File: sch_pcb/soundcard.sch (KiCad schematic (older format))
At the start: 50 parts, among them U501 CM108B, U502 CM108B, U503 TUSB2036, Y501 6MHz

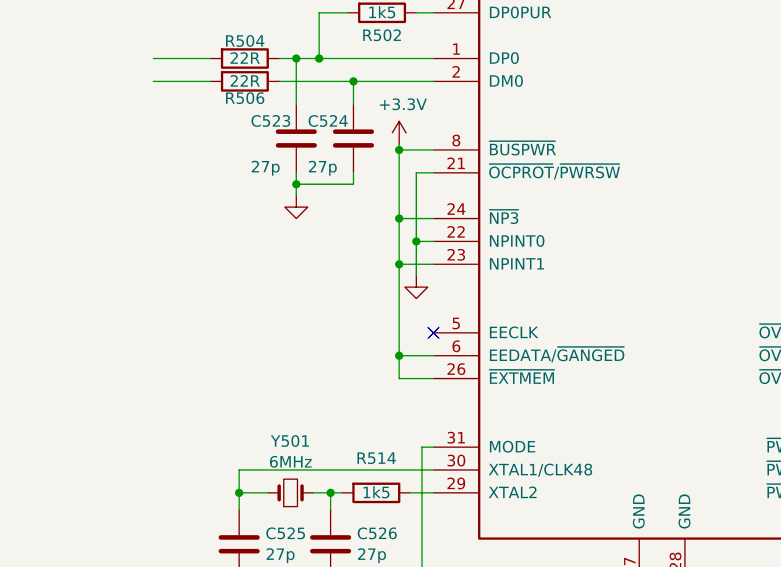
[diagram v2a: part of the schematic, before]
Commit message: Add files via upload
More routing of the PCB....  Slowly getting there.
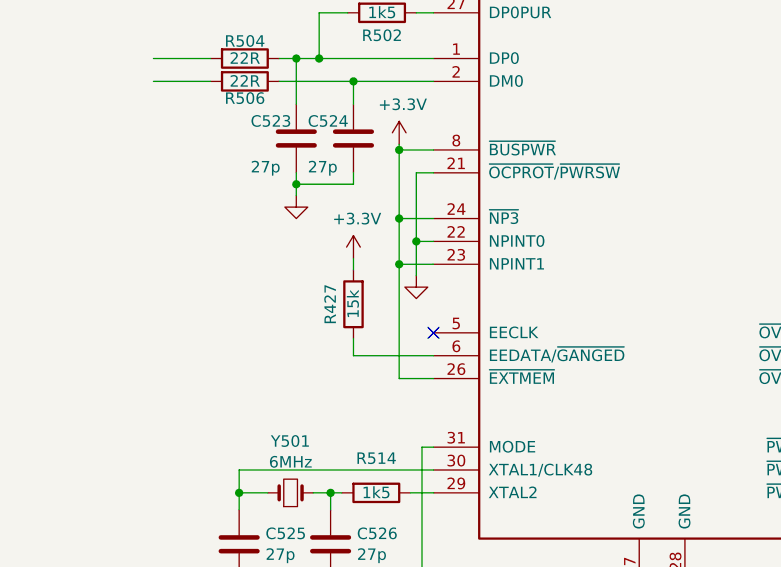
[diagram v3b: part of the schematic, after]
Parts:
- added R427: 15k, lib:smd0603, symbol R
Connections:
- wire segments 169 -> 171
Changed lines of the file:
@@
 LIBS:conn
 LIBS:PiPtr-cache
-EELAYER 25 0
+EELAYER 26 0
 EELAYER END
 $Descr A4 11693 8268
@@
 	9775 2125 9775 2200
 $Comp
-L GND #PWR0149
+L GND #PWR0148
 U 1 1 5968E48D
 P 9775 2200
-F 0 "#PWR0149" H 9775 1950 50  0001 C CNN
+F 0 "#PWR0148" H 9775 1950 50  0001 C CNN
 F 1 "GND" H 9780 2027 50  0001 C CNN
 F 2 "" H 9775 2200 50  0001 C CNN
@@
 $EndComp
 $Comp
-L GND #PWR0150
+L GND #PWR0149
 U 1 1 5968E4AC
 P 8575 4025
-F 0 "#PWR0150" H 8575 3775 50  0001 C CNN
+F 0 "#PWR0149" H 8575 3775 50  0001 C CNN
 F 1 "GND" H 8580 3852 50  0001 C CNN
 F 2 "" H 8575 4025 50  0001 C CNN
@@
 Connection ~ 8275 3925
 $Comp
-L GND #PWR0151
+L GND #PWR0150
 U 1 1 5968E5A1
 P 7100 3550
-F 0 "#PWR0151" H 7100 3300 50  0001 C CNN
+F 0 "#PWR0150" H 7100 3300 50  0001 C CNN
 F 1 "GND" H 7105 3377 50  0001 C CNN
 F 2 "" H 7100 3550 50  0001 C CNN
@@
 $EndComp
 $Comp
-L GND #PWR0152
+L GND #PWR0151
 U 1 1 5968EB73
 P 6925 1525
-F 0 "#PWR0152" H 6925 1275 50  0001 C CNN
+F 0 "#PWR0151" H 6925 1275 50  0001 C CNN
 F 1 "GND" H 6930 1352 50  0001 C CNN
 F 2 "" H 6925 1525 50  0001 C CNN
@@
 $EndComp
 $Comp
-L GND #PWR0153
+L GND #PWR0152
 U 1 1 5968F4FA
 P 9775 3975
-F 0 "#PWR0153" H 9775 3725 50  0001 C CNN
+F 0 "#PWR0152" H 9775 3725 50  0001 C CNN
 F 1 "GND" H 9780 3802 50  0001 C CNN
 F 2 "" H 9775 3975 50  0001 C CNN
@@
 Connection ~ 6200 4000
 $Comp
-L GND #PWR0154
+L GND #PWR0153
 U 1 1 5968FE8C
 P 6200 4075
-F 0 "#PWR0154" H 6200 3825 50  0001 C CNN
+F 0 "#PWR0153" H 6200 3825 50  0001 C CNN
 F 1 "GND" H 6205 3902 50  0001 C CNN
 F 2 "" H 6200 4075 50  0001 C CNN
@@
 	4525 2125 4525 2200
 $Comp
-L GND #PWR0155
+L GND #PWR0154
 U 1 1 596926E6
 P 4525 2200
-F 0 "#PWR0155" H 4525 1950 50  0001 C CNN
+F 0 "#PWR0154" H 4525 1950 50  0001 C CNN
 F 1 "GND" H 4530 2027 50  0001 C CNN
 F 2 "" H 4525 2200 50  0001 C CNN
@@
 $EndComp
 $Comp
-L GND #PWR0156
+L GND #PWR0155
 U 1 1 596926EC
 P 3325 4025
-F 0 "#PWR0156" H 3325 3775 50  0001 C CNN
+F 0 "#PWR0155" H 3325 3775 50  0001 C CNN
 F 1 "GND" H 3330 3852 50  0001 C CNN
 F 2 "" H 3325 4025 50  0001 C CNN
@@
 Connection ~ 3025 3925
 $Comp
-L GND #PWR0157
+L GND #PWR0156
 U 1 1 596926FD
 P 1850 3550
-F 0 "#PWR0157" H 1850 3300 50  0001 C CNN
+F 0 "#PWR0156" H 1850 3300 50  0001 C CNN
 F 1 "GND" H 1855 3377 50  0001 C CNN
 F 2 "" H 1850 3550 50  0001 C CNN
@@
 $EndComp
 $Comp
-L GND #PWR0158
+L GND #PWR0157
 U 1 1 5969275D
 P 4525 3975
-F 0 "#PWR0158" H 4525 3725 50  0001 C CNN
+F 0 "#PWR0157" H 4525 3725 50  0001 C CNN
 F 1 "GND" H 4530 3802 50  0001 C CNN
 F 2 "" H 4525 3975 50  0001 C CNN
@@
 Connection ~ 950  4000
 $Comp
-L GND #PWR0159
+L GND #PWR0158
 U 1 1 59692791
 P 950 4075
-F 0 "#PWR0159" H 950 3825 50  0001 C CNN
+F 0 "#PWR0158" H 950 3825 50  0001 C CNN
 F 1 "GND" H 955 3902 50  0001 C CNN
 F 2 "" H 950 4075 50  0001 C CNN
@@
 $EndComp
 $Comp
-L GND #PWR0160
+L GND #PWR0159
 U 1 1 59695E9D
 P 1750 7675
-F 0 "#PWR0160" H 1750 7425 50  0001 C CNN
+F 0 "#PWR0159" H 1750 7425 50  0001 C CNN
 F 1 "GND" H 1755 7502 50  0001 C CNN
 F 2 "" H 1750 7675 50  0001 C CNN
@@
 NoConn ~ 2600 6500
 $Comp
-L +3.3V #PWR0161
+L +3.3V #PWR0160
 U 1 1 596973F4
 P 2450 5675
-F 0 "#PWR0161" H 2450 5525 50  0001 C CNN
+F 0 "#PWR0160" H 2450 5525 50  0001 C CNN
 F 1 "+3.3V" H 2465 5848 50  0000 C CNN
 F 2 "" H 2450 5675 50  0001 C CNN
@@
 $EndComp
 $Comp
-L GND #PWR0162
+L GND #PWR0161
 U 1 1 596977E6
 P 2525 6250
-F 0 "#PWR0162" H 2525 6000 50  0001 C CNN
+F 0 "#PWR0161" H 2525 6000 50  0001 C CNN
 F 1 "GND" H 2530 6077 50  0001 C CNN
 F 2 "" H 2525 6250 50  0001 C CNN
@@
 Wire Wire Line
 	2525 5800 2600 5800
-Wire Wire Line
-	2600 6600 2450 6600
-Connection ~ 2450 6600
 Wire Wire Line
 	2600 5700 2450 5700
@@
 $EndComp
 $Comp
-L GND #PWR0163
+L GND #PWR0162
 U 1 1 596992AD
 P 2000 5900
-F 0 "#PWR0163" H 2000 5650 50  0001 C CNN
+F 0 "#PWR0162" H 2000 5650 50  0001 C CNN
 F 1 "GND" H 2005 5727 50  0001 C CNN
 F 2 "" H 2000 5900 50  0001 C CNN
@@
 $EndComp
 $Comp
-L GND #PWR0164
+L GND #PWR0163
 U 1 1 5969AB36
 P 4400 4400
-F 0 "#PWR0164" H 4400 4150 50  0001 C CNN
+F 0 "#PWR0163" H 4400 4150 50  0001 C CNN
 F 1 "GND" H 4405 4227 50  0001 C CNN
 F 2 "" H 4400 4400 50  0001 C CNN
@@
 Connection ~ 3500 4325
 $Comp
-L +3.3V #PWR0165
+L +3.3V #PWR0164
 U 1 1 5969B1EB
 P 3500 4250
-F 0 "#PWR0165" H 3500 4100 50  0001 C CNN
+F 0 "#PWR0164" H 3500 4100 50  0001 C CNN
 F 1 "+3.3V" H 3515 4423 50  0000 C CNN
 F 2 "" H 3500 4250 50  0001 C CNN
@@
 NoConn ~ 4600 6100
 Wire Wire Line
-	2600 6200 2450 6200
+	2450 6200 2600 6200
 Connection ~ 2450 6200
 Wire Wire Line
@@
 Connection ~ 5750 6300
 $Comp
-L GND #PWR0166
+L GND #PWR0165
 U 1 1 596A65D7
 P 5750 6375
-F 0 "#PWR0166" H 5750 6125 50  0001 C CNN
+F 0 "#PWR0165" H 5750 6125 50  0001 C CNN
 F 1 "GND" H 5755 6202 50  0001 C CNN
 F 2 "" H 5750 6375 50  0001 C CNN
@@
 $EndComp
 $Comp
-L GND #PWR0167
+L GND #PWR0166
 U 1 1 596AA48C
 P 2200 4900
-F 0 "#PWR0167" H 2200 4650 50  0001 C CNN
+F 0 "#PWR0166" H 2200 4650 50  0001 C CNN
 F 1 "GND" H 2205 4727 50  0001 C CNN
 F 2 "" H 2200 4900 50  0001 C CNN
@@
 $EndComp
 $Comp
-L +3.3V #PWR0168
+L +3.3V #PWR0167
 U 1 1 596AA4FD
 P 2200 4075
-F 0 "#PWR0168" H 2200 3925 50  0001 C CNN
+F 0 "#PWR0167" H 2200 3925 50  0001 C CNN
 F 1 "+3.3V" H 2215 4248 50  0000 C CNN
 F 2 "" H 2200 4075 50  0001 C CNN
@@
 	4775 6125 4775 6050
 $Comp
-L +3.3V #PWR0169
+L +3.3V #PWR0168
 U 1 1 5978D82E
 P 4775 6050
-F 0 "#PWR0169" H 4775 5900 50  0001 C CNN
+F 0 "#PWR0168" H 4775 5900 50  0001 C CNN
 F 1 "+3.3V" H 4790 6223 50  0000 C CNN
 F 2 "" H 4775 6050 50  0001 C CNN
@@
 	10050 3225 10150 3225
 $Comp
-L +5V #PWR0170
+L +5V #PWR0169
 U 1 1 597E7379
 P 6025 850
-F 0 "#PWR0170" H 6025 700 50  0001 C CNN
+F 0 "#PWR0169" H 6025 700 50  0001 C CNN
 F 1 "+5V" H 6025 990 50  0000 C CNN
 F 2 "" H 6025 850 50  0001 C CNN
@@
 $EndComp
 $Comp
-L +5V #PWR0171
+L +5V #PWR0170
 U 1 1 597E7689
 P 875 825
-F 0 "#PWR0171" H 875 675 50  0001 C CNN
+F 0 "#PWR0170" H 875 675 50  0001 C CNN
 F 1 "+5V" H 875 965 50  0000 C CNN
 F 2 "" H 875 825 50  0001 C CNN
@@
 $EndComp
 $Comp
-L +5V #PWR0172
+L +5V #PWR0171
 U 1 1 597C24B2
 P 3075 850
-F 0 "#PWR0172" H 3075 700 50  0001 C CNN
+F 0 "#PWR0171" H 3075 700 50  0001 C CNN
 F 1 "+5V" H 3075 990 50  0000 C CNN
 F 2 "" H 3075 850 50  0001 C CNN
@@
 Connection ~ 9850 1375
 $Comp
-L GND #PWR0173
+L GND #PWR0172
 U 1 1 597C4F1B
 P 9850 1475
-F 0 "#PWR0173" H 9850 1225 50  0001 C CNN
+F 0 "#PWR0172" H 9850 1225 50  0001 C CNN
 F 1 "GND" H 9855 1302 50  0001 C CNN
 F 2 "" H 9850 1475 50  0001 C CNN
@@
 $EndComp
 $Comp
-L GND #PWR0174
+L GND #PWR0173
 U 1 1 597C5606
 P 4750 1450
-F 0 "#PWR0174" H 4750 1200 50  0001 C CNN
+F 0 "#PWR0173" H 4750 1200 50  0001 C CNN
 F 1 "GND" H 4755 1277 50  0001 C CNN
 F 2 "" H 4750 1450 50  0001 C CNN
@@
 Connection ~ 1300 925
 $Comp
-L GND #PWR0175
+L GND #PWR0174
 U 1 1 597C7ACB
 P 1300 1475
-F 0 "#PWR0175" H 1300 1225 50  0001 C CNN
+F 0 "#PWR0174" H 1300 1225 50  0001 C CNN
 F 1 "GND" H 1305 1302 50  0001 C CNN
 F 2 "" H 1300 1475 50  0001 C CNN
@@
 	2775 925  2775 1025
 $Comp
-L +5V #PWR0176
+L +5V #PWR0175
 U 1 1 5982DF1C
 P 8325 850
-F 0 "#PWR0176" H 8325 700 50  0001 C CNN
+F 0 "#PWR0175" H 8325 700 50  0001 C CNN
 F 1 "+5V" H 8325 990 50  0000 C CNN
 F 2 "" H 8325 850 50  0001 C CNN
@@
 Connection ~ 8325 925
 $Comp
-L PWR_FLAG #FLG0177
+L PWR_FLAG #FLG0176
 U 1 1 5982F39E
 P 6925 925
-F 0 "#FLG0177" H 6925 1000 50  0001 C CNN
+F 0 "#FLG0176" H 6925 1000 50  0001 C CNN
 F 1 "PWR_FLAG" H 6925 1099 50  0001 C CNN
 F 2 "" H 6925 925 50  0001 C CNN
@@
 $EndComp
 $Comp
-L PWR_FLAG #FLG0178
+L PWR_FLAG #FLG0177
 U 1 1 5982F5DB
 P 1750 925
-F 0 "#FLG0178" H 1750 1000 50  0001 C CNN
+F 0 "#FLG0177" H 1750 1000 50  0001 C CNN
 F 1 "PWR_FLAG" H 1750 1099 50  0001 C CNN
 F 2 "" H 1750 925 50  0001 C CNN
@@
 	1    0    0    -1
 $EndComp
+$Comp
+L R R427
+U 1 1 59814A45
+P 2250 6375
+F 0 "R427" V 2350 6375 50  0000 C CNN
+F 1 "15k" V 2250 6375 50  0000 C CNN
+F 2 "lib:smd0603" V 2180 6375 50  0001 C CNN
+F 3 "" H 2250 6375 50  0001 C CNN
+	1    2250 6375
+	-1   0    0    1
+$EndComp
+$Comp
+L +3.3V #PWR0401
+U 1 1 59814E80
+P 2250 6175
+F 0 "#PWR0401" H 2250 6025 50  0001 C CNN
+F 1 "+3.3V" H 2265 6348 50  0000 C CNN
+F 2 "" H 2250 6175 50  0001 C CNN
+F 3 "" H 2250 6175 50  0001 C CNN
+	1    2250 6175
+	1    0    0    -1
+$EndComp
+Wire Wire Line
+	2250 6175 2250 6225
+Wire Wire Line
+	2600 6600 2250 6600
+Wire Wire Line
+	2250 6600 2250 6525
 $EndSCHEMATC

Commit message: Add files via upload
Remove OLED connector
Remove extra bypass cap from third EEPOT
More routing - got the soundcards and usb hub done.  Only remaining big section is the DC-DC.  Still a bit of pain-in-the-tuchas traces that need to sneak across the board...
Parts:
- renumbered R427 to R517
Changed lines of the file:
@@
 $EndComp
 $Comp
-L R R427
+L R R517
 U 1 1 59814A45
 P 2250 6375
-F 0 "R427" V 2350 6375 50  0000 C CNN
+F 0 "R517" V 2350 6375 50  0000 C CNN
 F 1 "15k" V 2250 6375 50  0000 C CNN
 F 2 "lib:smd0603" V 2180 6375 50  0001 C CNN

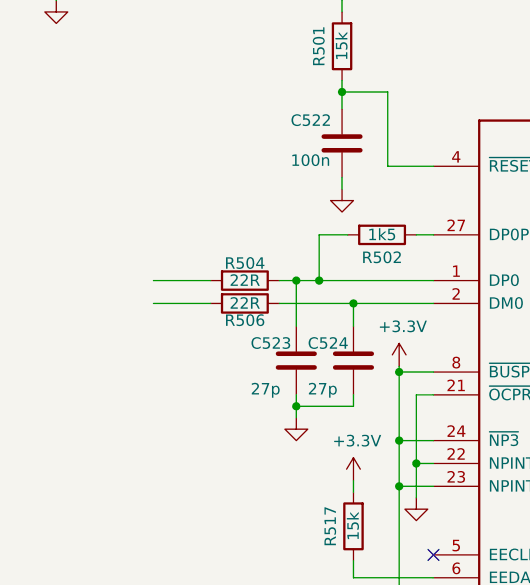
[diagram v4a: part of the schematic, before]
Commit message: Add files via upload
Add USB connector.  Pull back corner of board for it so the main board connector is around the same depth as the one on the Pi
Finish moving all refdes to avoid pads, other silk, and vias
Some routing cleanup
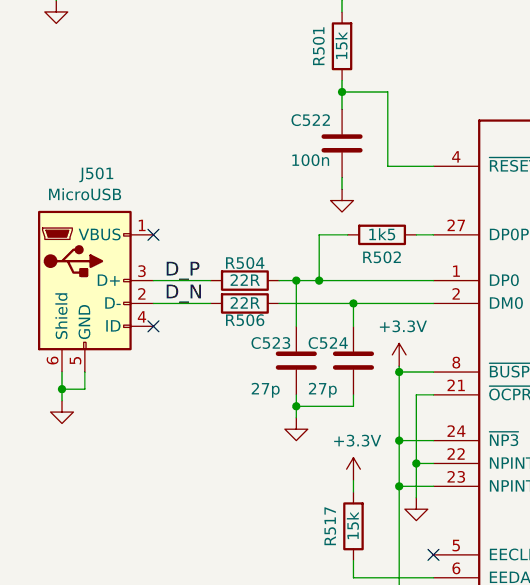
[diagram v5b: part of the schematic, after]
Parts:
- added J501: MicroUSB, lib:USB_Micro-B, symbol USB_OTG
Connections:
- net labels added: D_N, D_P
- wire segments 171 -> 174
- no-connect marks 56 -> 58
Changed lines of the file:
@@
 $Descr A4 11693 8268
 encoding utf-8
-Sheet 4 5
+Sheet 5 5
 Title ""
 Date ""
@@
 	9775 2125 9775 2200
 $Comp
-L GND #PWR0148
+L GND #PWR0182
 U 1 1 5968E48D
 P 9775 2200
-F 0 "#PWR0148" H 9775 1950 50  0001 C CNN
+F 0 "#PWR0182" H 9775 1950 50  0001 C CNN
 F 1 "GND" H 9780 2027 50  0001 C CNN
 F 2 "" H 9775 2200 50  0001 C CNN
@@
 $EndComp
 $Comp
-L GND #PWR0149
+L GND #PWR0183
 U 1 1 5968E4AC
 P 8575 4025
-F 0 "#PWR0149" H 8575 3775 50  0001 C CNN
+F 0 "#PWR0183" H 8575 3775 50  0001 C CNN
 F 1 "GND" H 8580 3852 50  0001 C CNN
 F 2 "" H 8575 4025 50  0001 C CNN
@@
 Connection ~ 8275 3925
 $Comp
-L GND #PWR0150
+L GND #PWR0184
 U 1 1 5968E5A1
 P 7100 3550
-F 0 "#PWR0150" H 7100 3300 50  0001 C CNN
+F 0 "#PWR0184" H 7100 3300 50  0001 C CNN
 F 1 "GND" H 7105 3377 50  0001 C CNN
 F 2 "" H 7100 3550 50  0001 C CNN
@@
 $EndComp
 $Comp
-L GND #PWR0151
+L GND #PWR0185
 U 1 1 5968EB73
 P 6925 1525
-F 0 "#PWR0151" H 6925 1275 50  0001 C CNN
+F 0 "#PWR0185" H 6925 1275 50  0001 C CNN
 F 1 "GND" H 6930 1352 50  0001 C CNN
 F 2 "" H 6925 1525 50  0001 C CNN
@@
 $EndComp
 $Comp
-L GND #PWR0152
+L GND #PWR0186
 U 1 1 5968F4FA
 P 9775 3975
-F 0 "#PWR0152" H 9775 3725 50  0001 C CNN
+F 0 "#PWR0186" H 9775 3725 50  0001 C CNN
 F 1 "GND" H 9780 3802 50  0001 C CNN
 F 2 "" H 9775 3975 50  0001 C CNN
@@
 Connection ~ 6200 4000
 $Comp
-L GND #PWR0153
+L GND #PWR0187
 U 1 1 5968FE8C
 P 6200 4075
-F 0 "#PWR0153" H 6200 3825 50  0001 C CNN
+F 0 "#PWR0187" H 6200 3825 50  0001 C CNN
 F 1 "GND" H 6205 3902 50  0001 C CNN
 F 2 "" H 6200 4075 50  0001 C CNN
@@
 	4525 2125 4525 2200
 $Comp
-L GND #PWR0154
+L GND #PWR0188
 U 1 1 596926E6
 P 4525 2200
-F 0 "#PWR0154" H 4525 1950 50  0001 C CNN
+F 0 "#PWR0188" H 4525 1950 50  0001 C CNN
 F 1 "GND" H 4530 2027 50  0001 C CNN
 F 2 "" H 4525 2200 50  0001 C CNN
@@
 $EndComp
 $Comp
-L GND #PWR0155
+L GND #PWR0189
 U 1 1 596926EC
 P 3325 4025
-F 0 "#PWR0155" H 3325 3775 50  0001 C CNN
+F 0 "#PWR0189" H 3325 3775 50  0001 C CNN
 F 1 "GND" H 3330 3852 50  0001 C CNN
 F 2 "" H 3325 4025 50  0001 C CNN
@@
 Connection ~ 3025 3925
 $Comp
-L GND #PWR0156
+L GND #PWR0190
 U 1 1 596926FD
 P 1850 3550
-F 0 "#PWR0156" H 1850 3300 50  0001 C CNN
+F 0 "#PWR0190" H 1850 3300 50  0001 C CNN
 F 1 "GND" H 1855 3377 50  0001 C CNN
 F 2 "" H 1850 3550 50  0001 C CNN
@@
 $EndComp
 $Comp
-L GND #PWR0157
+L GND #PWR0191
 U 1 1 5969275D
 P 4525 3975
-F 0 "#PWR0157" H 4525 3725 50  0001 C CNN
+F 0 "#PWR0191" H 4525 3725 50  0001 C CNN
 F 1 "GND" H 4530 3802 50  0001 C CNN
 F 2 "" H 4525 3975 50  0001 C CNN
@@
 Connection ~ 950  4000
 $Comp
-L GND #PWR0158
+L GND #PWR0192
 U 1 1 59692791
 P 950 4075
-F 0 "#PWR0158" H 950 3825 50  0001 C CNN
+F 0 "#PWR0192" H 950 3825 50  0001 C CNN
 F 1 "GND" H 955 3902 50  0001 C CNN
 F 2 "" H 950 4075 50  0001 C CNN
@@
 $EndComp
 $Comp
-L GND #PWR0159
+L GND #PWR0193
 U 1 1 59695E9D
 P 1750 7675
-F 0 "#PWR0159" H 1750 7425 50  0001 C CNN
+F 0 "#PWR0193" H 1750 7425 50  0001 C CNN
 F 1 "GND" H 1755 7502 50  0001 C CNN
 F 2 "" H 1750 7675 50  0001 C CNN
@@
 NoConn ~ 2600 6500
 $Comp
-L +3.3V #PWR0160
+L +3.3V #PWR0194
 U 1 1 596973F4
 P 2450 5675
-F 0 "#PWR0160" H 2450 5525 50  0001 C CNN
+F 0 "#PWR0194" H 2450 5525 50  0001 C CNN
 F 1 "+3.3V" H 2465 5848 50  0000 C CNN
 F 2 "" H 2450 5675 50  0001 C CNN
@@
 $EndComp
 $Comp
-L GND #PWR0161
+L GND #PWR0195
 U 1 1 596977E6
 P 2525 6250
-F 0 "#PWR0161" H 2525 6000 50  0001 C CNN
+F 0 "#PWR0195" H 2525 6000 50  0001 C CNN
 F 1 "GND" H 2530 6077 50  0001 C CNN
 F 2 "" H 2525 6250 50  0001 C CNN
@@
 $EndComp
 $Comp
-L GND #PWR0162
+L GND #PWR0196
 U 1 1 596992AD
 P 2000 5900
-F 0 "#PWR0162" H 2000 5650 50  0001 C CNN
+F 0 "#PWR0196" H 2000 5650 50  0001 C CNN
 F 1 "GND" H 2005 5727 50  0001 C CNN
 F 2 "" H 2000 5900 50  0001 C CNN
@@
 $EndComp
 $Comp
-L GND #PWR0163
+L GND #PWR0197
 U 1 1 5969AB36
 P 4400 4400
-F 0 "#PWR0163" H 4400 4150 50  0001 C CNN
+F 0 "#PWR0197" H 4400 4150 50  0001 C CNN
 F 1 "GND" H 4405 4227 50  0001 C CNN
 F 2 "" H 4400 4400 50  0001 C CNN
@@
 Connection ~ 3500 4325
 $Comp
-L +3.3V #PWR0164
+L +3.3V #PWR0198
 U 1 1 5969B1EB
 P 3500 4250
-F 0 "#PWR0164" H 3500 4100 50  0001 C CNN
+F 0 "#PWR0198" H 3500 4100 50  0001 C CNN
 F 1 "+3.3V" H 3515 4423 50  0000 C CNN
 F 2 "" H 3500 4250 50  0001 C CNN
@@
 Connection ~ 5750 6300
 $Comp
-L GND #PWR0165
+L GND #PWR0199
 U 1 1 596A65D7
 P 5750 6375
-F 0 "#PWR0165" H 5750 6125 50  0001 C CNN
+F 0 "#PWR0199" H 5750 6125 50  0001 C CNN
 F 1 "GND" H 5755 6202 50  0001 C CNN
 F 2 "" H 5750 6375 50  0001 C CNN
@@
 $EndComp
 $Comp
-L GND #PWR0166
+L GND #PWR0200
 U 1 1 596AA48C
 P 2200 4900
-F 0 "#PWR0166" H 2200 4650 50  0001 C CNN
+F 0 "#PWR0200" H 2200 4650 50  0001 C CNN
 F 1 "GND" H 2205 4727 50  0001 C CNN
 F 2 "" H 2200 4900 50  0001 C CNN
@@
 $EndComp
 $Comp
-L +3.3V #PWR0167
+L +3.3V #PWR0201
 U 1 1 596AA4FD
 P 2200 4075
-F 0 "#PWR0167" H 2200 3925 50  0001 C CNN
+F 0 "#PWR0201" H 2200 3925 50  0001 C CNN
 F 1 "+3.3V" H 2215 4248 50  0000 C CNN
 F 2 "" H 2200 4075 50  0001 C CNN
@@
 	4775 6125 4775 6050
 $Comp
-L +3.3V #PWR0168
+L +3.3V #PWR0202
 U 1 1 5978D82E
 P 4775 6050
-F 0 "#PWR0168" H 4775 5900 50  0001 C CNN
+F 0 "#PWR0202" H 4775 5900 50  0001 C CNN
 F 1 "+3.3V" H 4790 6223 50  0000 C CNN
 F 2 "" H 4775 6050 50  0001 C CNN
@@
 	10050 3225 10150 3225
 $Comp
-L +5V #PWR0169
+L +5V #PWR0203
 U 1 1 597E7379
 P 6025 850
-F 0 "#PWR0169" H 6025 700 50  0001 C CNN
+F 0 "#PWR0203" H 6025 700 50  0001 C CNN
 F 1 "+5V" H 6025 990 50  0000 C CNN
 F 2 "" H 6025 850 50  0001 C CNN
@@
 $EndComp
 $Comp
-L +5V #PWR0170
+L +5V #PWR0204
 U 1 1 597E7689
 P 875 825
-F 0 "#PWR0170" H 875 675 50  0001 C CNN
+F 0 "#PWR0204" H 875 675 50  0001 C CNN
 F 1 "+5V" H 875 965 50  0000 C CNN
 F 2 "" H 875 825 50  0001 C CNN
@@
 $EndComp
 $Comp
-L +5V #PWR0171
+L +5V #PWR0205
 U 1 1 597C24B2
 P 3075 850
-F 0 "#PWR0171" H 3075 700 50  0001 C CNN
+F 0 "#PWR0205" H 3075 700 50  0001 C CNN
 F 1 "+5V" H 3075 990 50  0000 C CNN
 F 2 "" H 3075 850 50  0001 C CNN
@@
 Connection ~ 9850 1375
 $Comp
-L GND #PWR0172
+L GND #PWR0206
 U 1 1 597C4F1B
 P 9850 1475
-F 0 "#PWR0172" H 9850 1225 50  0001 C CNN
+F 0 "#PWR0206" H 9850 1225 50  0001 C CNN
 F 1 "GND" H 9855 1302 50  0001 C CNN
 F 2 "" H 9850 1475 50  0001 C CNN
@@
 $EndComp
 $Comp
-L GND #PWR0173
+L GND #PWR0207
 U 1 1 597C5606
 P 4750 1450
-F 0 "#PWR0173" H 4750 1200 50  0001 C CNN
+F 0 "#PWR0207" H 4750 1200 50  0001 C CNN
 F 1 "GND" H 4755 1277 50  0001 C CNN
 F 2 "" H 4750 1450 50  0001 C CNN
@@
 Connection ~ 1300 925
 $Comp
-L GND #PWR0174
+L GND #PWR0208
 U 1 1 597C7ACB
 P 1300 1475
-F 0 "#PWR0174" H 1300 1225 50  0001 C CNN
+F 0 "#PWR0208" H 1300 1225 50  0001 C CNN
 F 1 "GND" H 1305 1302 50  0001 C CNN
 F 2 "" H 1300 1475 50  0001 C CNN
@@
 	2775 925  2775 1025
 $Comp
-L +5V #PWR0175
+L +5V #PWR0209
 U 1 1 5982DF1C
 P 8325 850
-F 0 "#PWR0175" H 8325 700 50  0001 C CNN
+F 0 "#PWR0209" H 8325 700 50  0001 C CNN
 F 1 "+5V" H 8325 990 50  0000 C CNN
 F 2 "" H 8325 850 50  0001 C CNN
@@
 Connection ~ 8325 925
 $Comp
-L PWR_FLAG #FLG0176
+L PWR_FLAG #FLG0210
 U 1 1 5982F39E
 P 6925 925
-F 0 "#FLG0176" H 6925 1000 50  0001 C CNN
+F 0 "#FLG0210" H 6925 1000 50  0001 C CNN
 F 1 "PWR_FLAG" H 6925 1099 50  0001 C CNN
 F 2 "" H 6925 925 50  0001 C CNN
@@
 $EndComp
 $Comp
-L PWR_FLAG #FLG0177
+L PWR_FLAG #FLG0211
 U 1 1 5982F5DB
 P 1750 925
-F 0 "#FLG0177" H 1750 1000 50  0001 C CNN
+F 0 "#FLG0211" H 1750 1000 50  0001 C CNN
 F 1 "PWR_FLAG" H 1750 1099 50  0001 C CNN
 F 2 "" H 1750 925 50  0001 C CNN
@@
 $EndComp
 $Comp
-L +3.3V #PWR0401
+L +3.3V #PWR0212
 U 1 1 59814E80
 P 2250 6175
-F 0 "#PWR0401" H 2250 6025 50  0001 C CNN
+F 0 "#PWR0212" H 2250 6025 50  0001 C CNN
 F 1 "+3.3V" H 2265 6348 50  0000 C CNN
 F 2 "" H 2250 6175 50  0001 C CNN
@@
 Wire Wire Line
 	2250 6600 2250 6525
+$Comp
+L USB_OTG J501
+U 1 1 598CA320
+P 1075 5300
+F 0 "J501" H 1130 5767 50  0000 C CNN
+F 1 "MicroUSB" H 1075 5675 50  0000 C CNN
+F 2 "lib:USB_Micro-B" H 1225 5250 50  0001 C CNN
+F 3 "Amphenol_10118194-0001LF" H 1225 5250 50  0001 C CNN
+	1    1075 5300
+	1    0    0    -1
+$EndComp
+NoConn ~ 1375 5100
+NoConn ~ 1375 5500
+$Comp
+L GND #PWR0213
+U 1 1 598CAADE
+P 975 5825
+F 0 "#PWR0213" H 975 5575 50  0001 C CNN
+F 1 "GND" H 980 5652 50  0001 C CNN
+F 2 "" H 975 5825 50  0001 C CNN
+F 3 "" H 975 5825 50  0001 C CNN
+	1    975  5825
+	1    0    0    -1
+$EndComp
+Wire Wire Line
+	975  5700 975  5825
+Wire Wire Line
+	1075 5700 1075 5775
+Wire Wire Line
+	1075 5775 975  5775
+Connection ~ 975  5775
+Text Label 1425 5300 0    60   ~ 0
+D_P
+Text Label 1425 5400 0    60   ~ 0
+D_N
 $EndSCHEMATC
